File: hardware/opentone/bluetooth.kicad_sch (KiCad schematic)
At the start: 1 part

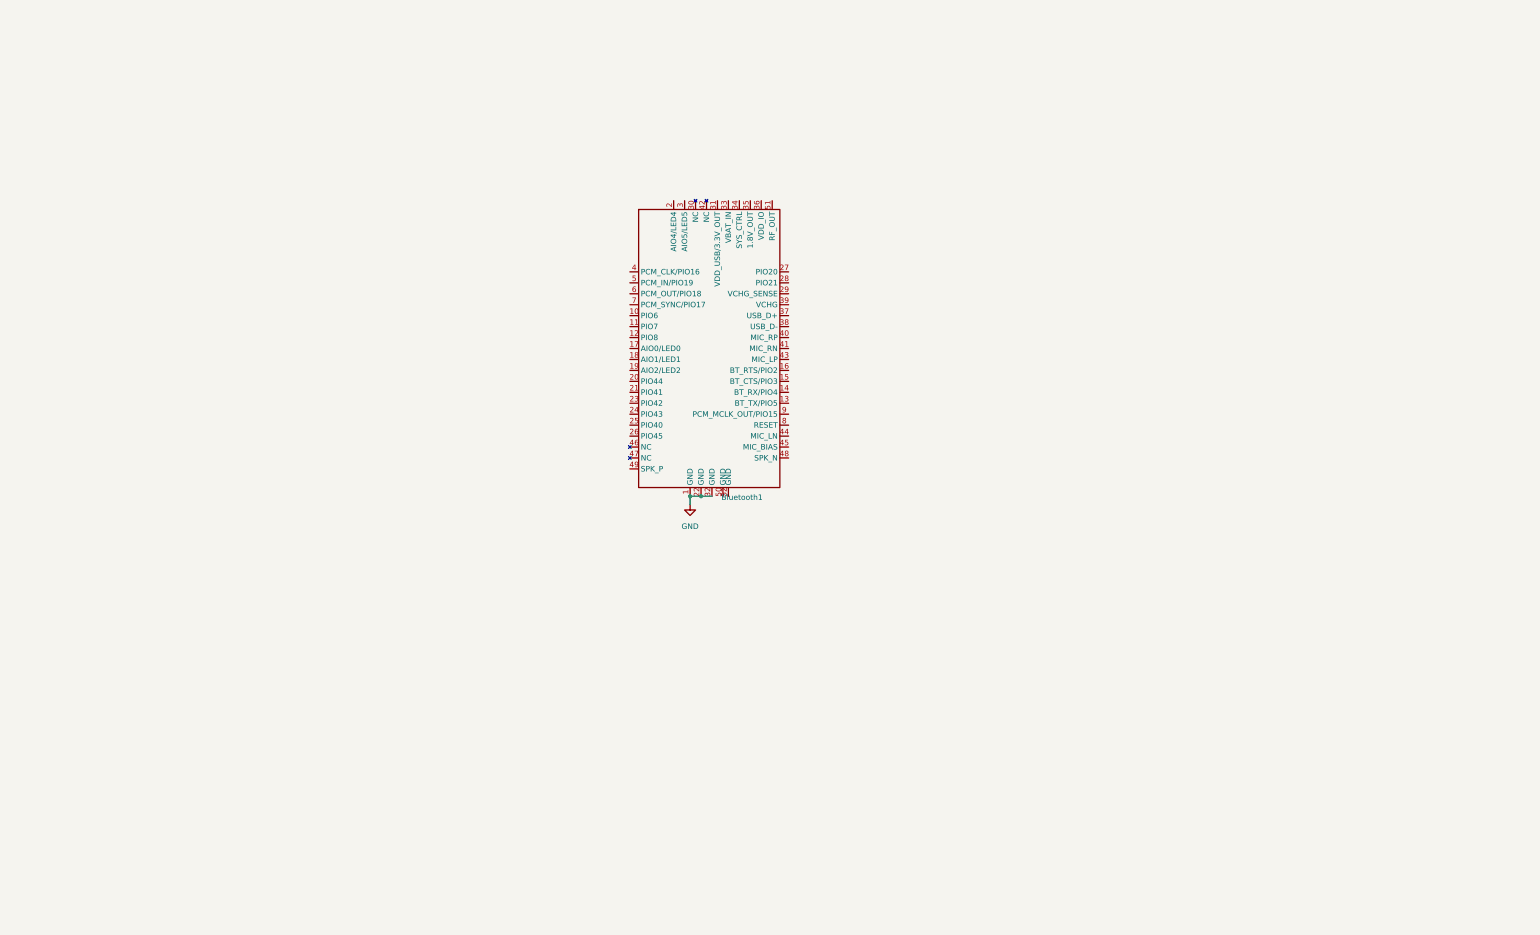
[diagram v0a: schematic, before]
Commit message: devboard audio and bluetooth schema
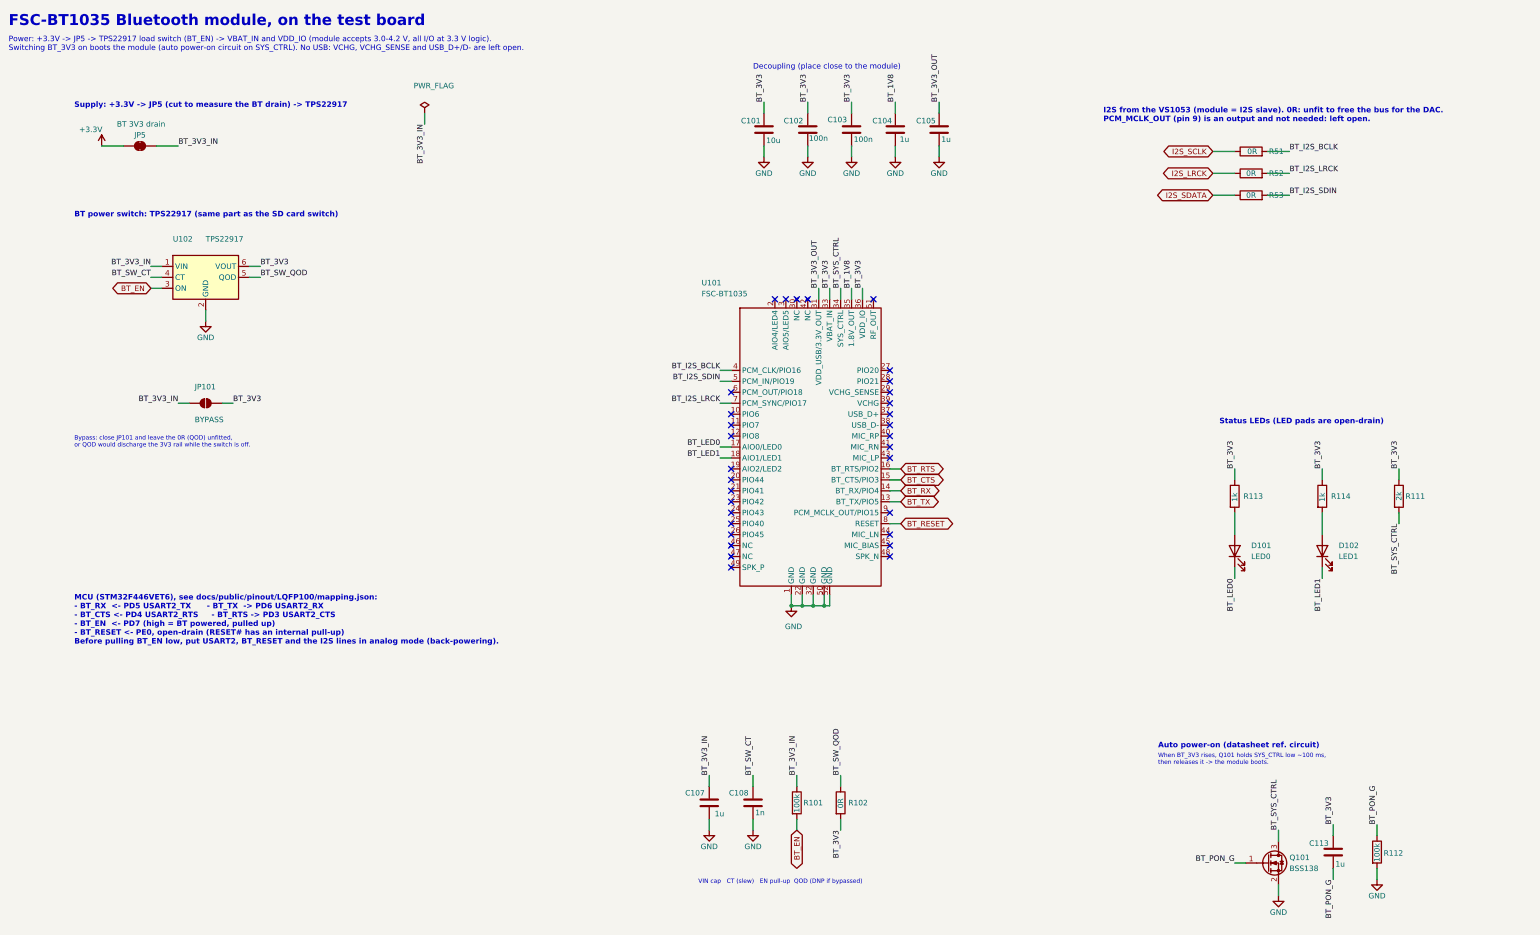
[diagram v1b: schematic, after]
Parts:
- removed Bluetooth1: ~, opentone:fsc-bt1035, symbol opentone:FSC-BT1035
- added C101: 10u, Capacitor_SMD:C_0805_2012Metric, symbol Device:C
- added C102, C103: 100n, Capacitor_SMD:C_0805_2012Metric, symbol Device:C
- added C104, C105, C107, C113: 1u, Capacitor_SMD:C_0805_2012Metric, symbol Device:C
- added C108: 1n, Capacitor_SMD:C_0805_2012Metric, symbol Device:C
- added D101: LED0, LED_SMD:LED_0805_2012Metric, symbol Device:LED
- added D102: LED1, LED_SMD:LED_0805_2012Metric, symbol Device:LED
- added JP101: BYPASS, Jumper:SolderJumper-2_P1.3mm_Open_RoundedPad1.0x1.5mm, symbol Jumper:SolderJumper_2_Open
- added JP5: BT 3V3 drain, Jumper:SolderJumper-2_P1.3mm_Bridged_RoundedPad1.0x1.5mm, symbol Jumper:SolderJumper_2_Bridged
- added Q101: BSS138, Package_TO_SOT_SMD:SOT-23, symbol Transistor_FET:BSS138
- added R101, R112: 100k, Resistor_SMD:R_0805_2012Metric, symbol Device:R
- added R102, R51, R52, R53: 0R, Resistor_SMD:R_0805_2012Metric, symbol Device:R
- added R111: 2k, Resistor_SMD:R_0805_2012Metric, symbol Device:R
- added R113, R114: 1k, Resistor_SMD:R_0805_2012Metric, symbol Device:R
- added U101: FSC-BT1035, opentone:fsc-bt1035, symbol opentone:FSC-BT1035
- added U102: TPS22917, Package_TO_SOT_SMD:SOT-23-6, symbol Power_Management:TPS22917DBV
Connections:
- net GND: now also C101.2, C102.2, C103.2, C104.2, C105.2, C107.2, C108.2, Q101.2 (S), R112.2, U101.1 (GND), U101.22 (GND), U101.32 (GND), U101.50 (GND), U101.52 (GND), U102.2 (GND)
- new net: D102.2 (A), R114.2
- new net: D101.2 (A), R113.2
- new net +3.3V: JP5.1 (A)
- new net BT_1V8: C104.1, U101.35 (1.8V_OUT)
- new net BT_3V3: C101.1, C102.1, C103.1, C113.1, JP101.2 (B), R102.2, R111.1, R113.1, R114.1, U101.33 (VBAT_IN), U101.36 (VDD_IO), U102.6 (VOUT)
- new net BT_3V3_IN: C107.1, JP101.1 (A), JP5.2 (B), R101.1, U102.1 (VIN)
- new net BT_3V3_OUT: C105.1, U101.31 (VDD_USB/3.3V_OUT)
- new net BT_CTS: U101.15 (BT_CTS/PIO3)
- new net BT_EN: R101.2, U102.3 (ON)
- new net BT_I2S_BCLK: R51.2, U101.4 (PCM_CLK/PIO16)
- new net BT_I2S_LRCK: R52.2, U101.7 (PCM_SYNC/PIO17)
- new net BT_I2S_SDIN: R53.2, U101.5 (PCM_IN/PIO19)
- new net BT_LED0: D101.1 (K), U101.17 (AIO0/LED0)
- new net BT_LED1: D102.1 (K), U101.18 (AIO1/LED1)
- new net BT_PON_G: C113.2, Q101.1 (G), R112.1
- new net BT_RESET: U101.8 (RESET)
- new net BT_RTS: U101.16 (BT_RTS/PIO2)
- new net BT_RX: U101.14 (BT_RX/PIO4)
- new net BT_SW_CT: C108.1, U102.4 (CT)
- new net BT_SW_QOD: R102.1, U102.5 (QOD)
- new net BT_SYS_CTRL: Q101.3 (D), R111.2, U101.34 (SYS_CTRL)
- new net BT_TX: U101.13 (BT_TX/PIO5)
- new net I2S_LRCK: R52.1
- new net I2S_SCLK: R51.1
- new net I2S_SDATA: R53.1
- no-connect marks 0 -> 32
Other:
- note added: "Auto power-on (datasheet ref. circuit)"
- note added: "BT power switch: TPS22917 (same part as the SD card switch)"
- note added: "Bypass: close JP101 and leave the 0R (QOD) unfitted, or QOD would discharge the 3V3 rail while the switch is off."
- note added: "Decoupling (place close to the module)"
- note added: "FSC-BT1035 Bluetooth module, on the test board"
- note added: "I2S from the VS1053 (module = I2S slave). 0R: unfit to free the bus for the DAC. PCM_MCLK_OUT (pin 9) is an output and not needed: left open."
- note added: "MCU (STM32F446VET6), see docs/public/pinout/LQFP100/mapping.json: - BT_RX <- PD5 USART2_TX - BT_TX -> PD6 USART2_RX - BT_CTS <- PD4 USART2_RTS - BT_RTS -> PD3 USART2_CTS - BT_EN <- PD7 (high = BT powered, pulled up) - BT_RESET <- PE0, open-drain (RESET# has an internal pull-up) Before pulling BT_EN low, put USART2, BT_RESET and the I2S lines in analog mode (back-powering)."
- note added: "Power: +3.3V -> JP5 -> TPS22917 load switch (BT_EN) -> VBAT_IN and VDD_IO (module accepts 3.0-4.2 V, all I/O at 3.3 V logic). Switching BT_3V3 on boots the module (auto power-on circuit on SYS_CTRL). No USB: VCHG, VCHG_SENSE and USB_D+/D- are left open."
- note added: "Status LEDs (LED pads are open-drain)"
- note added: "Supply: +3.3V -> JP5 (cut to measure the BT drain) -> TPS22917"
- note added: "VIN cap CT (slew) EN pull-up QOD (DNP if bypassed)"
- note added: "When BT_3V3 rises, Q101 holds SYS_CTRL low ~100 ms, then releases it -> the module boots."
- title: (none) -> Bluetooth (FSC-BT1035)

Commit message: added sd card, haptic, updated old parts and set a datasheet and MPN to all parts
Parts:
- C101: footprint Capacitor_SMD:C_0805_2012Metric -> Capacitor_SMD:C_0603_1608Metric; LCSC (none) -> C19702; Manufacturer (none) -> Samsung Electro-Mechanics; Part number (none) -> CL10A106KP8NNNC
- C102, C103: footprint Capacitor_SMD:C_0805_2012Metric -> Capacitor_SMD:C_0603_1608Metric; LCSC (none) -> C14663; Manufacturer (none) -> YAGEO; Part number (none) -> CC0603KRX7R9BB104
- C104, C105, C107, C113: footprint Capacitor_SMD:C_0805_2012Metric -> Capacitor_SMD:C_0603_1608Metric; LCSC (none) -> C15849; Manufacturer (none) -> Samsung Electro-Mechanics; Part number (none) -> CL10A105KB8NNNC
- C108: footprint Capacitor_SMD:C_0805_2012Metric -> Capacitor_SMD:C_0603_1608Metric; LCSC (none) -> C1588; Manufacturer (none) -> Samsung Electro-Mechanics; Part number (none) -> CL10B102KB8NNNC
- D101, D102: footprint LED_SMD:LED_0805_2012Metric -> LED_SMD:LED_0603_1608Metric; LCSC (none) -> C2286; Manufacturer (none) -> Hubei KENTO Elec; Part number (none) -> KT-0603R
- JP101, JP5: now left out of the parts list
- Q101: LCSC (none) -> C82045; Manufacturer (none) -> onsemi; Part number (none) -> BSS138LT1G
- R101, R112: footprint Resistor_SMD:R_0805_2012Metric -> Resistor_SMD:R_0603_1608Metric; LCSC (none) -> C25803; Manufacturer (none) -> UNI-ROYAL; Part number (none) -> 0603WAF1003T5E
- R102, R51, R52, R53: footprint Resistor_SMD:R_0805_2012Metric -> Resistor_SMD:R_0603_1608Metric; LCSC (none) -> C21189; Manufacturer (none) -> UNI-ROYAL; Part number (none) -> 0603WAF0000T5E
- R111: footprint Resistor_SMD:R_0805_2012Metric -> Resistor_SMD:R_0603_1608Metric; LCSC (none) -> C22975; Manufacturer (none) -> UNI-ROYAL; Part number (none) -> 0603WAF2001T5E
- R113, R114: footprint Resistor_SMD:R_0805_2012Metric -> Resistor_SMD:R_0603_1608Metric; LCSC (none) -> C21190; Manufacturer (none) -> UNI-ROYAL; Part number (none) -> 0603WAF1001T5E
- U101: Manufacturer (none) -> Feasycom; Part number (none) -> FSC-BT1035
- U102: Manufacturer (none) -> Texas Instruments; Part number (none) -> TPS22917DBVR

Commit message: updated BOM
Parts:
- C101: value 10u -> 10uF
- C102, C103: value 100n -> 100nF
- C104, C105, C107, C113: value 1u -> 1uF
- C108: value 1n -> 1nF
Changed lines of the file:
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@@
 			)
 		)
-		(property "Value" "100n"
+		(property "Value" "100nF"
 			(at 216.408 44.196 0)
 			(show_name no)
@@
 			)
 		)
-		(property "Value" "10u"
+		(property "Value" "10uF"
 			(at 196.088 44.45 0)
 			(show_name no)
@@
 			)
 		)
-		(property "Value" "100n"
+		(property "Value" "100nF"
 			(at 205.994 43.942 0)
 			(show_name no)
@@
 			)
 		)
-		(property "Value" "1u"
+		(property "Value" "1uF"
 			(at 328.168 212.344 0)
 			(show_name no)
@@
 			)
 		)
-		(property "Value" "1u"
+		(property "Value" "1uF"
 			(at 184.15 200.66 0)
 			(show_name no)
@@
 			)
 		)
-		(property "Value" "1u"
+		(property "Value" "1uF"
 			(at 227.076 44.196 0)
 			(show_name no)
@@
 			)
 		)
-		(property "Value" "1n"
+		(property "Value" "1nF"
 			(at 193.548 200.406 0)
 			(show_name no)
@@
 			)
 		)
-		(property "Value" "1u"
+		(property "Value" "1uF"
 			(at 236.728 44.196 0)
 			(show_name no)
